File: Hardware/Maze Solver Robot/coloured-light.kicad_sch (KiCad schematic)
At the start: 0 parts

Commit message: Add colour sensing circuit diagram
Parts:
- added R? (x2): A1050, OptoDevice:R_LDR_D6.4mm_P3.4mm_Vertical, symbol Sensor_Optical:A1050
- added RV? (x2): R_Potentiometer, symbol Device:R_Potentiometer
- added U? (x5): 4011, symbol 4xxx:4011
- added U? (x3): LM358, symbol Amplifier_Operational:LM358
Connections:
- new net: RV?.2, U?.5 (+)
- new net: U?.4, U?.8, U?.9
- new net: U?.12, U?.13, U?.3, U?.5
- new net: U?.6, U?.7
- new net: RV?.2, U?.3 (+)
- new net: U?.1, U?.1, U?.2
- new net GND: R?.1, R?.2, RV?.1, RV?.1, RV?.3, RV?.3, U?.14 (VDD), U?.4 (V-), U?.7 (VSS), U?.8 (V+)
- new net Green: U?.10
- new net Red: U?.11
- new net Vref: R?.1, R?.2, U?.2 (-), U?.6 (-)

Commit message: Add final changes
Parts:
- RV? (x2): value R_Potentiometer -> R_Potentiometer_10K
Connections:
- net GND: no longer R?.1, RV?.1, RV?.1, U?.14 (VDD), U?.8 (V+)
- new net 3.3V: R?.1, RV?.1, RV?.1, U?.14 (VDD), U?.8 (V+)
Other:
- note added: "Ambient light sensing. Placed at back of board"
- note added: "Coloured light sensing. Placed at front of board"
- moved on the sheet: R?, RV?, U?A, U?B, U?C, U?D, U?E

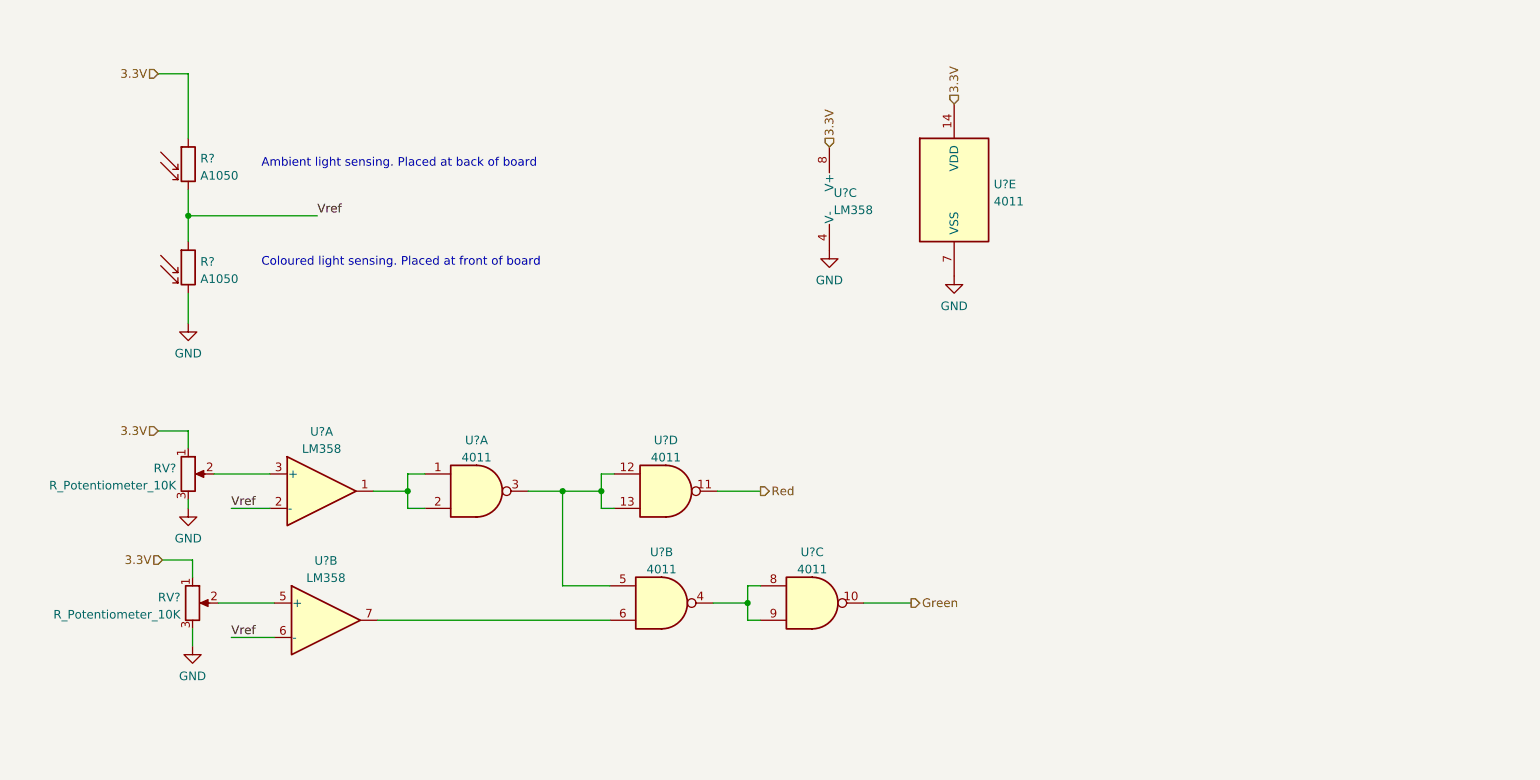
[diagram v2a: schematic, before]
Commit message: Add comments to schematics
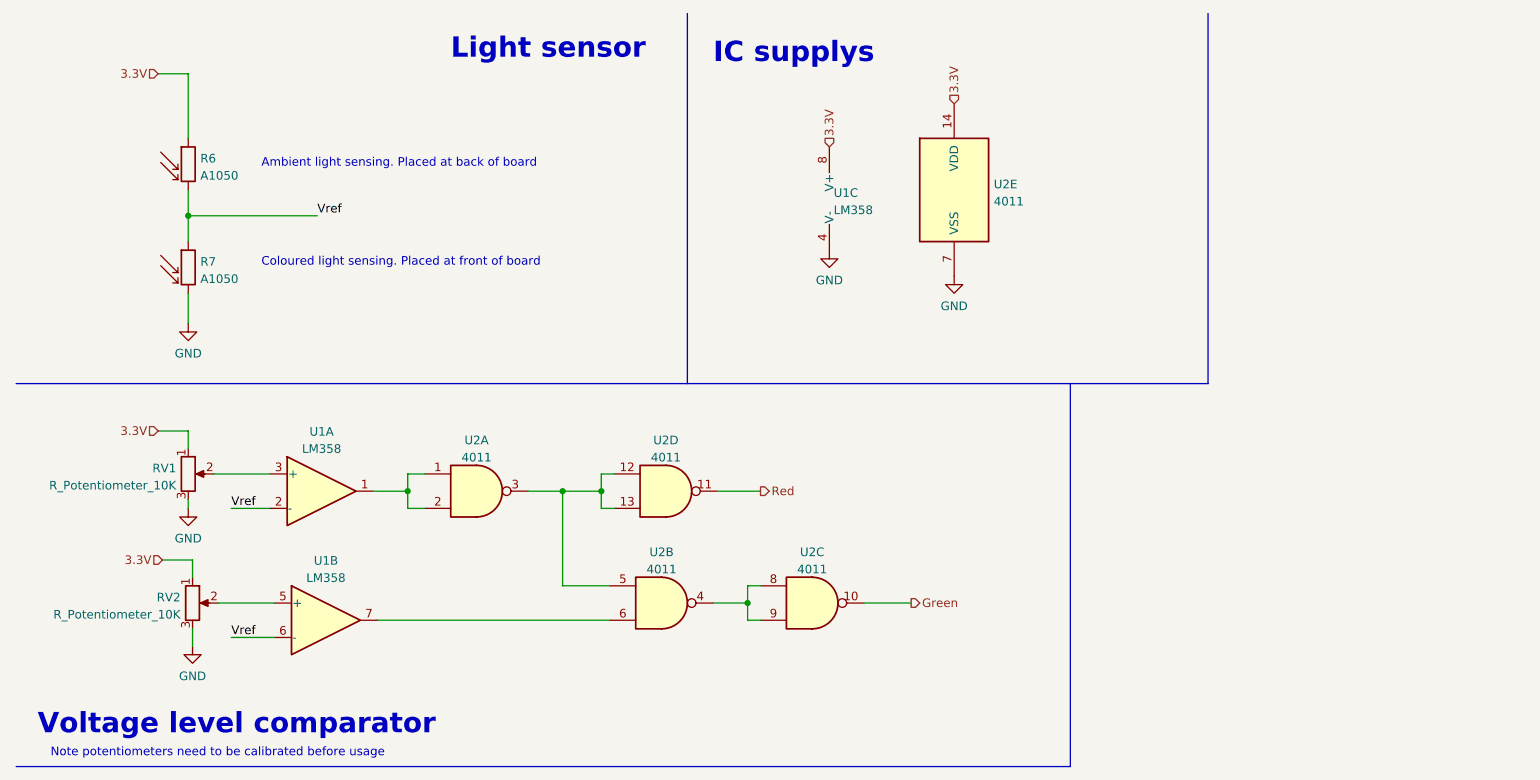
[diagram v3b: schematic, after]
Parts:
- gave numbers to parts that had none: 6
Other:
- note added: "IC supplys"
- note added: "Light sensor"
- note added: "Note potentiometers need to be calibrated before usage"
- note added: "Voltage level comparator"
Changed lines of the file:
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@@
+    (stroke (width 0) (type default) (color 0 0 0 0))
+  )
+  (polyline (pts (xy 12.065 123.19) (xy 167.64 123.19))
     (stroke (width 0) (type default) (color 0 0 0 0))
   )
@@
     (stroke (width 0) (type default) (color 0 0 0 0))
   )
+  (polyline (pts (xy 12.065 66.675) (xy 187.96 66.675))
+    (stroke (width 0) (type default) (color 0 0 0 0))
+  )
   (wire (pts (xy 37.465 20.955) (xy 37.465 30.48))
     (stroke (width 0) (type default) (color 0 0 0 0))
@@
     (stroke (width 0) (type default) (color 0 0 0 0))
   )
+  (polyline (pts (xy 167.64 123.19) (xy 167.64 66.675))
+    (stroke (width 0) (type default) (color 0 0 0 0))
+  )
   (wire (pts (xy 92.71 82.55) (xy 98.425 82.55))
     (stroke (width 0) (type default) (color 0 0 0 0))
@@
     (stroke (width 0) (type default) (color 0 0 0 0))
   )
+  (polyline (pts (xy 111.125 12.065) (xy 111.125 66.675))
+    (stroke (width 0) (type default) (color 0 0 0 0))
+  )
   (wire (pts (xy 115.57 82.55) (xy 121.92 82.55))
     (stroke (width 0) (type default) (color 0 0 0 0))
@@
     (stroke (width 0) (type default) (color 0 0 0 0))
   )
+  (polyline (pts (xy 187.96 12.065) (xy 187.96 66.675))
+    (stroke (width 0) (type default) (color 0 0 0 0))
+  )
   (wire (pts (xy 120.015 96.52) (xy 120.015 99.06))
     (stroke (width 0) (type default) (color 0 0 0 0))
@@
     (stroke (width 0) (type default) (color 0 0 0 0))
   )
+  (text "Voltage level comparator" (at 15.24 118.745 0)
+    (effects (font (size 3 3) bold) (justify left bottom))
+  )
   (text "Ambient light sensing. Placed at back of board" (at 48.26 34.925 0)
     (effects (font (size 1.27 1.27)) (justify left bottom))
   )
+  (text "Note potentiometers need to be calibrated before usage"
+    (at 17.145 121.92 0)
+    (effects (font (size 1.27 1.27)) (justify left bottom))
+  )
   (text "Coloured light sensing. Placed at front of board" (at 48.26 49.53 0)
     (effects (font (size 1.27 1.27)) (justify left bottom))
+  )
+  (text "Light sensor" (at 76.2 19.05 0)
+    (effects (font (size 3 3) bold) (justify left bottom))
+  )
+  (text "IC supplys" (at 114.935 19.685 0)
+    (effects (font (size 3 3) (thickness 0.6) bold) (justify left bottom))
   )
   (label "Vref" (at 43.815 85.09 0)
@@
   (symbol (lib_id "power:GND") (at 37.465 85.09 0) (unit 1)
     (in_bom yes) (on_board yes) (fields_autoplaced)
-    (property "Reference" "#PWR?" (id 0) (at 37.465 91.44 0)
+    (property "Reference" "#PWR05" (id 0) (at 37.465 91.44 0)
       (effects (font (size 1.27 1.27)) hide)
     )
@@
   (symbol (lib_id "power:GND") (at 132.08 46.99 0) (unit 1)
     (in_bom yes) (on_board yes) (fields_autoplaced)
-    (property "Reference" "#PWR?" (id 0) (at 132.08 53.34 0)
+    (property "Reference" "#PWR07" (id 0) (at 132.08 53.34 0)
       (effects (font (size 1.27 1.27)) hide)
     )
@@
   (symbol (lib_id "power:GND") (at 150.495 50.8 0) (unit 1)
     (in_bom yes) (on_board yes) (fields_autoplaced)
-    (property "Reference" "#PWR?" (id 0) (at 150.495 57.15 0)
+    (property "Reference" "#PWR08" (id 0) (at 150.495 57.15 0)
       (effects (font (size 1.27 1.27)) hide)
     )
@@
   (symbol (lib_id "Device:R_Potentiometer") (at 38.1 99.06 0) (unit 1)
     (in_bom yes) (on_board yes) (fields_autoplaced)
-    (property "Reference" "RV?" (id 0) (at 36.322 98.2253 0)
+    (property "Reference" "RV2" (id 0) (at 36.322 98.2253 0)
       (effects (font (size 1.27 1.27)) (justify right))
     )
@@
   (symbol (lib_id "Sensor_Optical:A1050") (at 37.465 34.29 0) (unit 1)
     (in_bom yes) (on_board yes) (fields_autoplaced)
-    (property "Reference" "R?" (id 0) (at 39.243 33.4553 0)
+    (property "Reference" "R6" (id 0) (at 39.243 33.4553 0)
       (effects (font (size 1.27 1.27)) (justify left))
     )
@@
   (symbol (lib_id "power:GND") (at 38.1 105.41 0) (unit 1)
     (in_bom yes) (on_board yes) (fields_autoplaced)
-    (property "Reference" "#PWR?" (id 0) (at 38.1 111.76 0)
+    (property "Reference" "#PWR06" (id 0) (at 38.1 111.76 0)
       (effects (font (size 1.27 1.27)) hide)
     )
@@
   (symbol (lib_id "4xxx:4011") (at 150.495 38.1 0) (unit 5)
     (in_bom yes) (on_board yes) (fields_autoplaced)
-    (property "Reference" "U?" (id 0) (at 156.337 37.2653 0)
+    (property "Reference" "U2" (id 0) (at 156.337 37.2653 0)
       (effects (font (size 1.27 1.27)) (justify left))
     )
@@
   (symbol (lib_id "4xxx:4011") (at 107.315 99.06 0) (unit 2)
     (in_bom yes) (on_board yes) (fields_autoplaced)
-    (property "Reference" "U?" (id 0) (at 107.315 91.5502 0))
+    (property "Reference" "U2" (id 0) (at 107.315 91.5502 0))
     (property "Value" "4011" (id 1) (at 107.315 94.0871 0))
     (property "Footprint" "" (id 2) (at 107.315 99.06 0)
@@
   (symbol (lib_id "4xxx:4011") (at 129.54 99.06 0) (unit 3)
     (in_bom yes) (on_board yes) (fields_autoplaced)
-    (property "Reference" "U?" (id 0) (at 129.54 91.5502 0))
+    (property "Reference" "U2" (id 0) (at 129.54 91.5502 0))
     (property "Value" "4011" (id 1) (at 129.54 94.0871 0))
     (property "Footprint" "" (id 2) (at 129.54 99.06 0)
@@
   (symbol (lib_id "Amplifier_Operational:LM358") (at 57.785 101.6 0) (unit 2)
     (in_bom yes) (on_board yes) (fields_autoplaced)
-    (property "Reference" "U?" (id 0) (at 57.785 92.8202 0))
+    (property "Reference" "U1" (id 0) (at 57.785 92.8202 0))
     (property "Value" "LM358" (id 1) (at 57.785 95.3571 0))
     (property "Footprint" "" (id 2) (at 57.785 101.6 0)
@@
   (symbol (lib_id "Device:R_Potentiometer") (at 37.465 80.01 0) (unit 1)
     (in_bom yes) (on_board yes)
-    (property "Reference" "RV?" (id 0) (at 35.6871 79.1753 0)
+    (property "Reference" "RV1" (id 0) (at 35.6871 79.1753 0)
       (effects (font (size 1.27 1.27)) (justify right))
     )
@@
   (symbol (lib_id "4xxx:4011") (at 80.01 82.55 0) (unit 1)
     (in_bom yes) (on_board yes) (fields_autoplaced)
-    (property "Reference" "U?" (id 0) (at 80.01 75.0402 0))
+    (property "Reference" "U2" (id 0) (at 80.01 75.0402 0))
     (property "Value" "4011" (id 1) (at 80.01 77.5771 0))
     (property "Footprint" "" (id 2) (at 80.01 82.55 0)
@@
   (symbol (lib_id "Amplifier_Operational:LM358") (at 57.15 82.55 0) (unit 1)
     (in_bom yes) (on_board yes) (fields_autoplaced)
-    (property "Reference" "U?" (id 0) (at 57.15 73.7702 0))
+    (property "Reference" "U1" (id 0) (at 57.15 73.7702 0))
     (property "Value" "LM358" (id 1) (at 57.15 76.3071 0))
     (property "Footprint" "" (id 2) (at 57.15 82.55 0)
@@
   (symbol (lib_id "power:GND") (at 37.465 57.785 0) (unit 1)
     (in_bom yes) (on_board yes) (fields_autoplaced)
-    (property "Reference" "#PWR?" (id 0) (at 37.465 64.135 0)
+    (property "Reference" "#PWR04" (id 0) (at 37.465 64.135 0)
       (effects (font (size 1.27 1.27)) hide)
     )
@@
   (symbol (lib_id "Sensor_Optical:A1050") (at 37.465 49.53 0) (unit 1)
     (in_bom yes) (on_board yes) (fields_autoplaced)
-    (property "Reference" "R?" (id 0) (at 39.243 48.6953 0)
+    (property "Reference" "R7" (id 0) (at 39.243 48.6953 0)
       (effects (font (size 1.27 1.27)) (justify left))
     )
@@
   (symbol (lib_id "4xxx:4011") (at 107.95 82.55 0) (unit 4)
     (in_bom yes) (on_board yes) (fields_autoplaced)
-    (property "Reference" "U?" (id 0) (at 107.95 75.0402 0))
+    (property "Reference" "U2" (id 0) (at 107.95 75.0402 0))
     (property "Value" "4011" (id 1) (at 107.95 77.5771 0))
     (property "Footprint" "" (id 2) (at 107.95 82.55 0)
@@
   (symbol (lib_id "Amplifier_Operational:LM358") (at 134.62 39.37 0) (unit 3)
     (in_bom yes) (on_board yes)
-    (property "Reference" "U?" (id 0) (at 132.715 38.5353 0)
-      (effects (font (size 1.27 1.27)) (justify left))
-    )
+    (property "Reference" "U1" (id 0) (at 132.715 38.5353 0)
+      (effects (font (size 1.27 1.27)) (justify left))
+    )

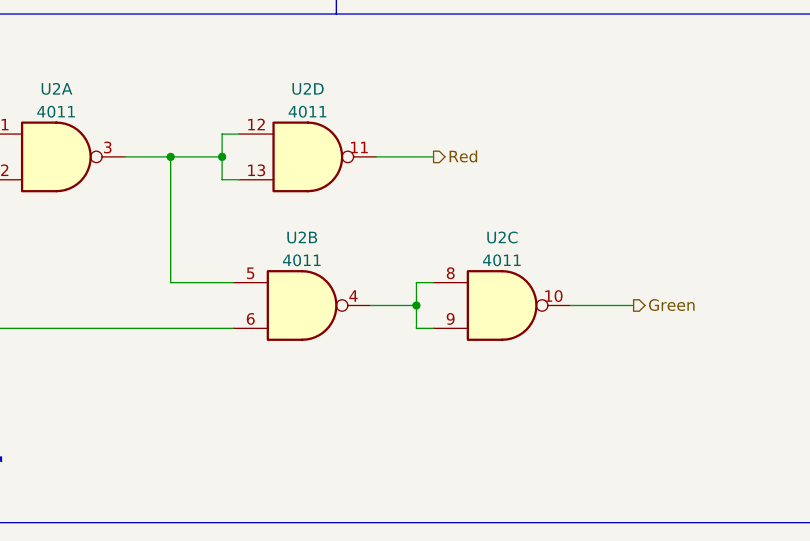
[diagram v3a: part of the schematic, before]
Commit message: Final changes to coloured light
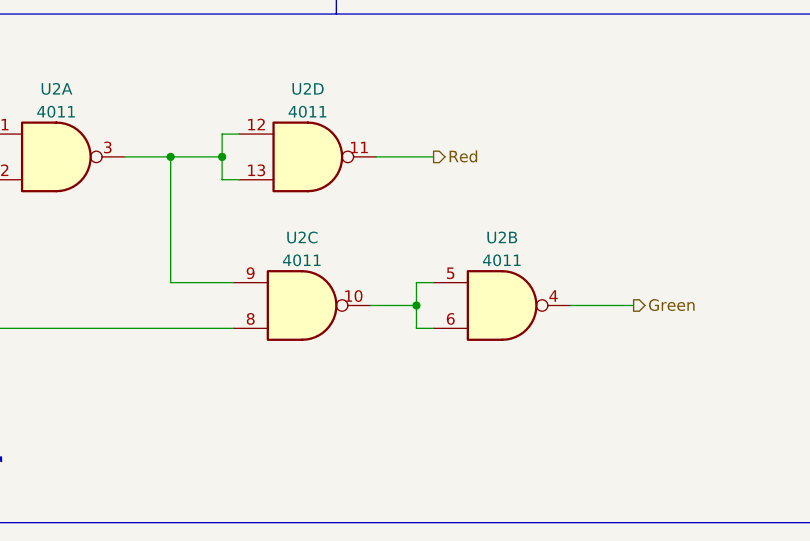
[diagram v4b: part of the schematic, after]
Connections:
- net Green: now also U2.4; no longer U2.10
- net at U2.12, U2.13, U2.3: now also U2.9; no longer U2.5
- net at U2.6: now also U2.10, U2.5; no longer U1.7
- new net: U1.7, U2.8
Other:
- moved on the sheet: U2B, U2C
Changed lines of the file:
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@@
     (pin "7")
   )
-  (symbol (lib_id "4xxx:4011") (at 107.315 99.06 0) (unit 2)
+  (symbol (lib_id "4xxx:4011") (at 129.54 99.06 0) (unit 2)
+    (in_bom yes) (on_board yes) (fields_autoplaced)
+    (property "Reference" "U2" (id 0) (at 129.54 91.5502 0))
+    (property "Value" "4011" (id 1) (at 129.54 94.0871 0))
+    (property "Footprint" "" (id 2) (at 129.54 99.06 0)
+      (effects (font (size 1.27 1.27)) hide)
+    )
+    (property "Datasheet" "http://www.intersil.com/content/dam/Intersil/documents/cd40/cd4011bms-12bms-23bms.pdf" (id 3) (at 129.54 99.06 0)
+      (effects (font (size 1.27 1.27)) hide)
+    )
+    (pin "4")
+    (pin "5")
+    (pin "6")
+  )
+  (symbol (lib_id "4xxx:4011") (at 107.315 99.06 0) (mirror x) (unit 3)
     (in_bom yes) (on_board yes) (fields_autoplaced)
     (property "Reference" "U2" (id 0) (at 107.315 91.5502 0))
@@
       (effects (font (size 1.27 1.27)) hide)
     )
-    (pin "4")
-    (pin "5")
-    (pin "6")
-  )
-  (symbol (lib_id "4xxx:4011") (at 129.54 99.06 0) (unit 3)
-    (in_bom yes) (on_board yes) (fields_autoplaced)
-    (property "Reference" "U2" (id 0) (at 129.54 91.5502 0))
-    (property "Value" "4011" (id 1) (at 129.54 94.0871 0))
-    (property "Footprint" "" (id 2) (at 129.54 99.06 0)
-      (effects (font (size 1.27 1.27)) hide)
-    )
-    (property "Datasheet" "http://www.intersil.com/content/dam/Intersil/documents/cd40/cd4011bms-12bms-23bms.pdf" (id 3) (at 129.54 99.06 0)
-      (effects (font (size 1.27 1.27)) hide)
-    )
